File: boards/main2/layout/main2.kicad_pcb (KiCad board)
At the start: 4 copper layers, 50 x 100 mm, 194 parts, among them IC1 STM32H725RGV6, IC2 LSM6DSVTR, IC6 STSPIN958TR, IC7 L6981C33DR, IC8 DRV8874PWPR, IC9 DRV8874PWPR, J1 B02B-PASK(LF)(SN), J2 HC-PZ127-7.2L-2x3PS, M1 B02B-PASK(LF)(SN), M2 B02B-PASK(LF)(SN), M3 B02B-PASK(LF)(SN), Q1 AO3400A, Q2 AO3400A, Q3 AO3400A, Q4 AO3400A, Q5 AO3400A, Q6 HSBB3072, Q9 AO3400A, SW1 DSHP04TJGER, SW2 GT-TC048B-H025-L1, SW3 GT-TC048B-H025-L1, SW4 SK-12D29-G060, U10 INA241A2IDGKR, U11 INA241A2IDGKR, U12 TLV9001IDBVR, U13 ESP32-C5-MINI-1-N4, U8 ADP7142ACPZN3.3-R7

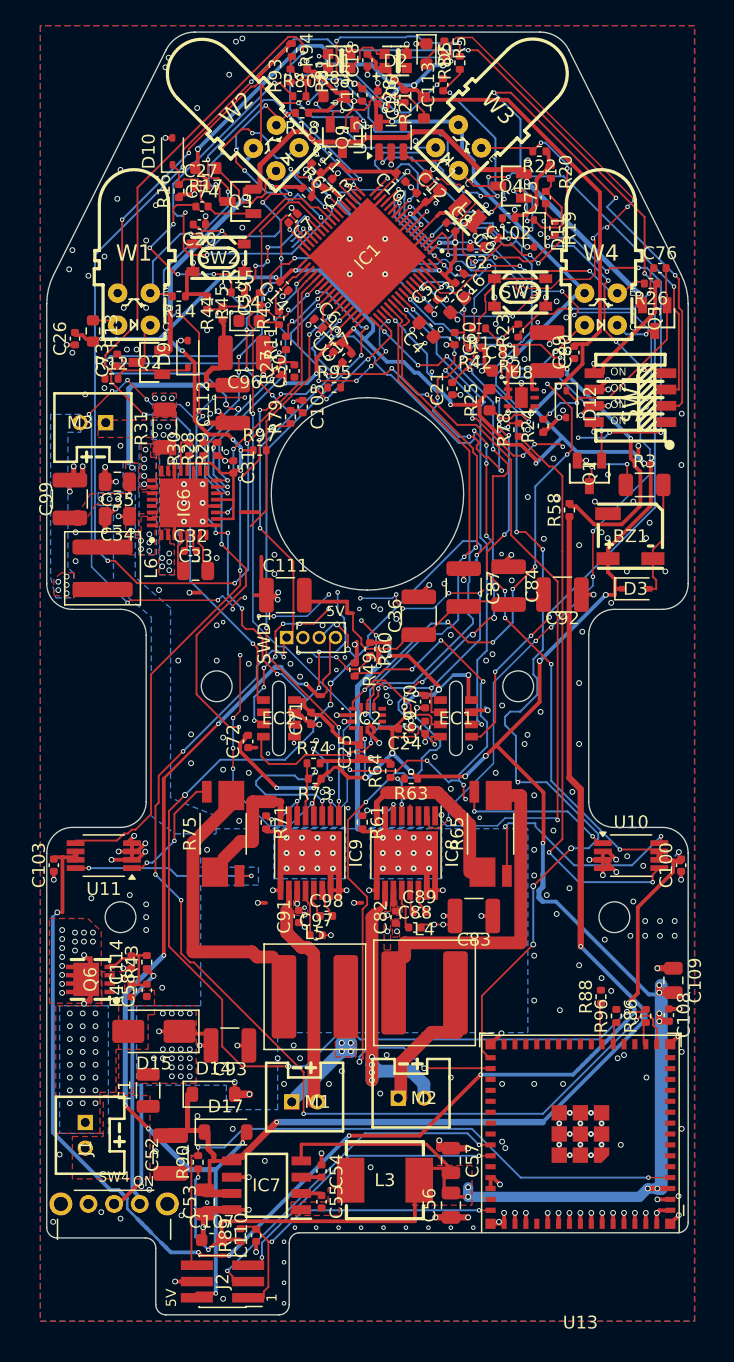
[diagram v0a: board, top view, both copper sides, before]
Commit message: 🚧 Move main2's C5 link to SPI3 on the STM32's rear-right face
SPI2's clock exists only on the STM32's left-side pins, so the link had to
cross every line leaving the rear-right face to reach the C5.

- The link moves to SPI3, a 3-wire master on MOSI with no IOSWP: SCK on
  PC10, DATA on PC12, CSn on PC11. The UART4 fallback stays on
  PC10/PC11 (AF8).
- The sensor bus moves to SPI2 on PB13/PB14/PB15.
- Fan_PWM moves to TIM14_CH1 on PA7, with the same 275 MHz clock and
  ARR. Button moves to PA11 and Fan_TOFF to PA12.
- CubeMX 6.18.1 accepts both the SPI and the UART4 configurations.
- Routed: all four link joins and the SPI_SCK join to EC2. DRC shows 0
  errors and 13 unconnected. Button, Fan_TOFF, Encoder_Right_ABI_B and
  Wall_Sensor_PWM_2 are open in the pocket behind the STM32's rear tip.
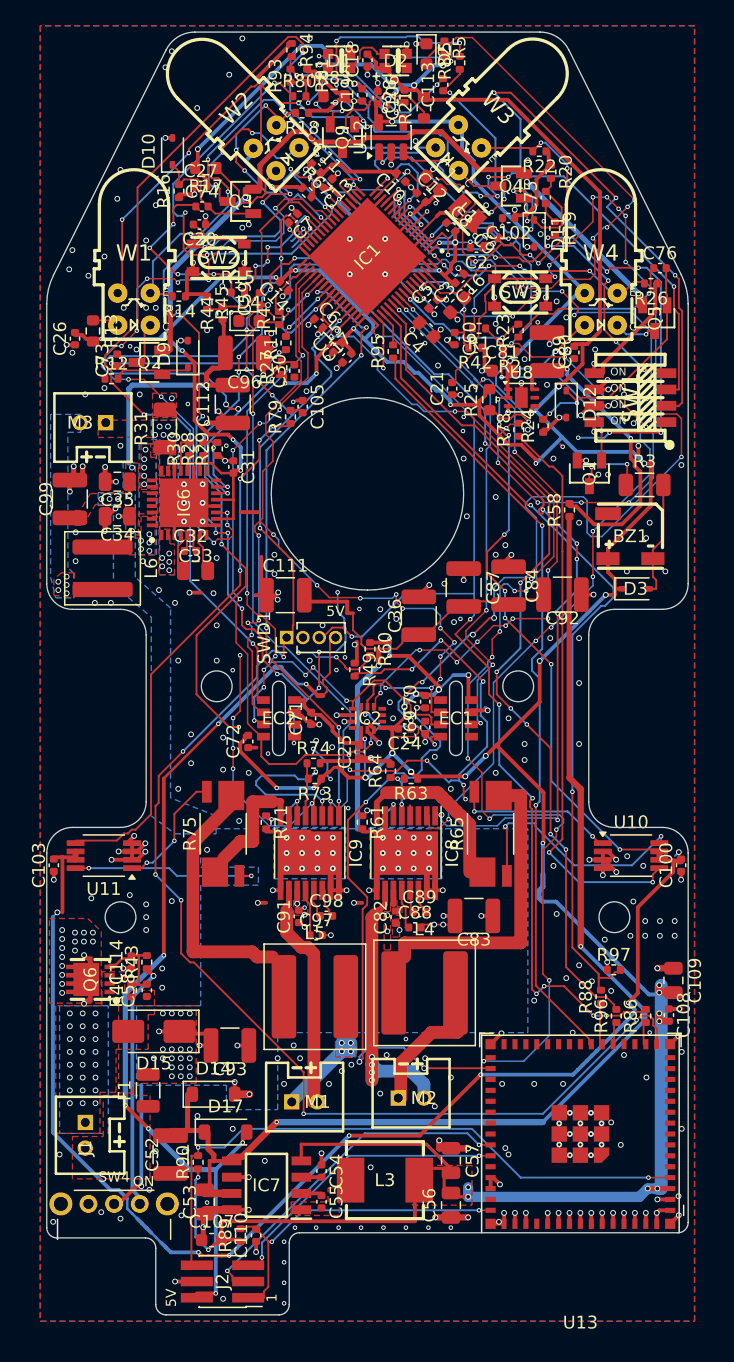
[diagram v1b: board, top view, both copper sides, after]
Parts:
- moved R97 49.0 mm to (167.7, 133.1)
- moved R95 5.39 mm to (150.5, 84.9), turned to 90 degrees
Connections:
- IC1 pad 26: Button -> Fan_PWM
- IC1 pad 37: Fan_TOFF -> SPI_SCK
- IC1 pad 38: ESP_DATA -> SPI_MISO
- IC1 pad 39: Fan_PWM -> SPI_MOSI
- IC1 pad 46: ESP_CSn -> Button
- IC1 pad 47: ESP_SCK -> Fan_TOFF
- IC1 pad 54: SPI_SCK -> ESP_SCK
- IC1 pad 55: SPI_MISO -> ESP_CSn
- IC1 pad 56: SPI_MOSI -> ESP_DATA
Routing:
- net Encoder_Right_ABI_B: track 168.1 -> 4.11 mm, vias 16 -> 1
- net ESP.ESP_SCK_IO: track 0.00 -> 60.7 mm, vias 0 -> 2
- net ESP_DATA: track 6.13 -> 66.5 mm, vias 0 -> 6
- net ESP_CSn: track 20.4 -> 64.7 mm
- net Reset: track 99.4 -> 140.8 mm, vias 10 -> 20
- net SWCLK: track 123.6 -> 83.5 mm, vias 12 -> 9
- net SPI_MISO: track 88.5 -> 57.3 mm, vias 21 -> 9
- net Fan_PWM: track 22.1 -> 52.7 mm, vias 2 -> 12
- net SPI_SCK: track 100.0 -> 72.2 mm, vias 25 -> 15
- net Fan_TOFF: track 21.5 -> 0.00 mm, vias 2 -> 0
- net Wall_Sensor_PWM_2: track 52.5 -> 34.9 mm, vias 13 -> 8
- net Current_Sensor_Right: track 49.9 -> 61.9 mm, vias 7 -> 11
- net Motor_Right_EN: track 66.7 -> 77.5 mm, vias 7 -> 8
- net IMU_SPI_CSn: track 39.8 -> 49.9 mm, vias 2 -> 12
- net Button: track 17.2 -> 8.23 mm, vias 2 -> 3
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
